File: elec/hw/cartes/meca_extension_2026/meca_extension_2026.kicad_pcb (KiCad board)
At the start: 4 copper layers, 126.2 x 84.5 mm, 189 parts, among them J1 2-1445051-3, J10 22053051, J11 B2B-XH-A, J12 22272021, J13 22053051, J14 22272031, J15 22272031, J16 5264-3P, J17 5267-3P, J18 5267-3P, J19 5267-3P, J2 B2B-XH-A, J20 5267-3P, J24 22053031, J25 22053031, J26 22053051, J27 22053041, J28 22053031, J29 22053031, J3 22272021, J4 22053051, J5 B2B-XH-A, J6 22272021, J7 22053051, J8 B2B-XH-A, J9 22272021, Q1 SI2310, Q10 SI2310, Q11 SI2310, Q12 2N7002, Q19 BSS84, Q2 SI2310, Q20 2N7002, Q3 2N7002, Q4 SI2310, Q5 SI2310, Q6 2N7002, Q7 SI2310, Q8 SI2310, Q9 2N7002, U1 TCA9548APWR, U11 LV14340DDAR, U2 PCA9535PW, U3 TLA2528IRTER, U4 TLV9061IDBVR, U5 TLV9061IDBVR, U6 TLV9061IDBVR, U7 TLV9061IDBVR, U8 74HCT238PW, U9 SN74LVC1T45DBV

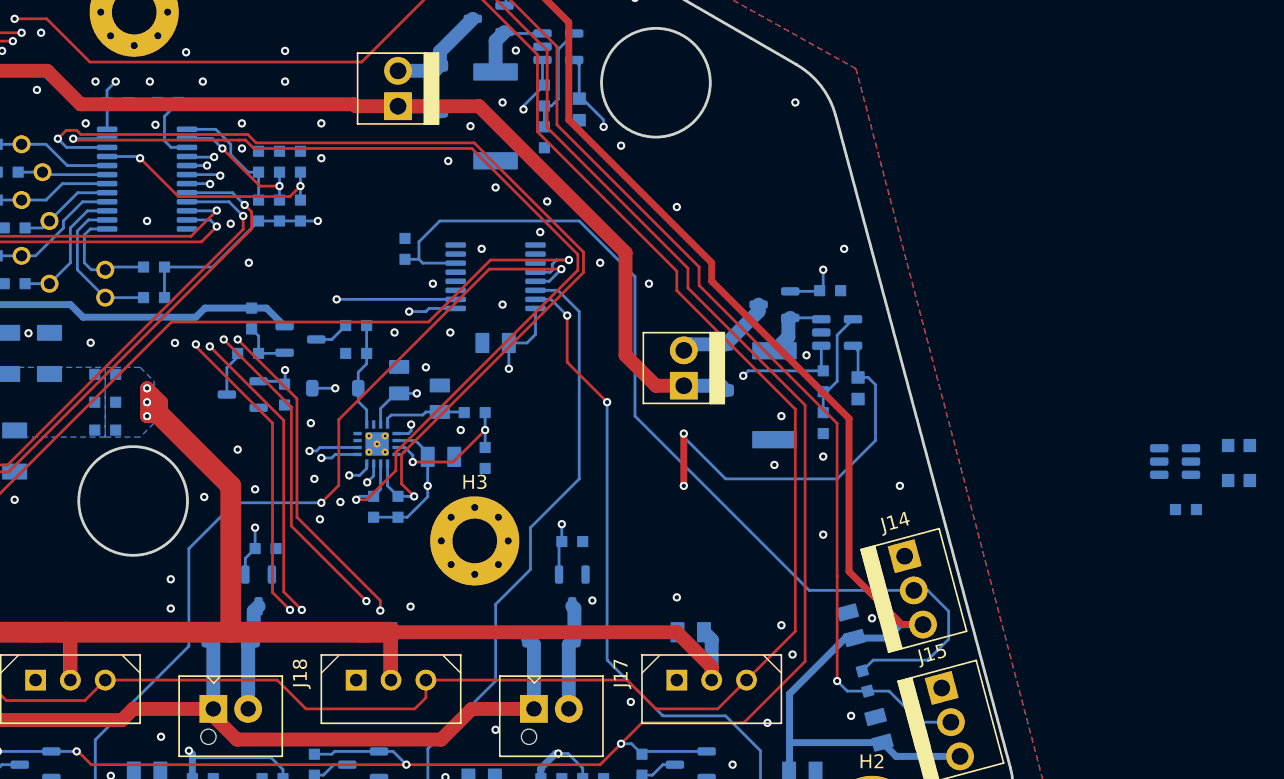
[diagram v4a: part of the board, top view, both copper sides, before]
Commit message: meca_extension : schematic correction and routing modified accordingly
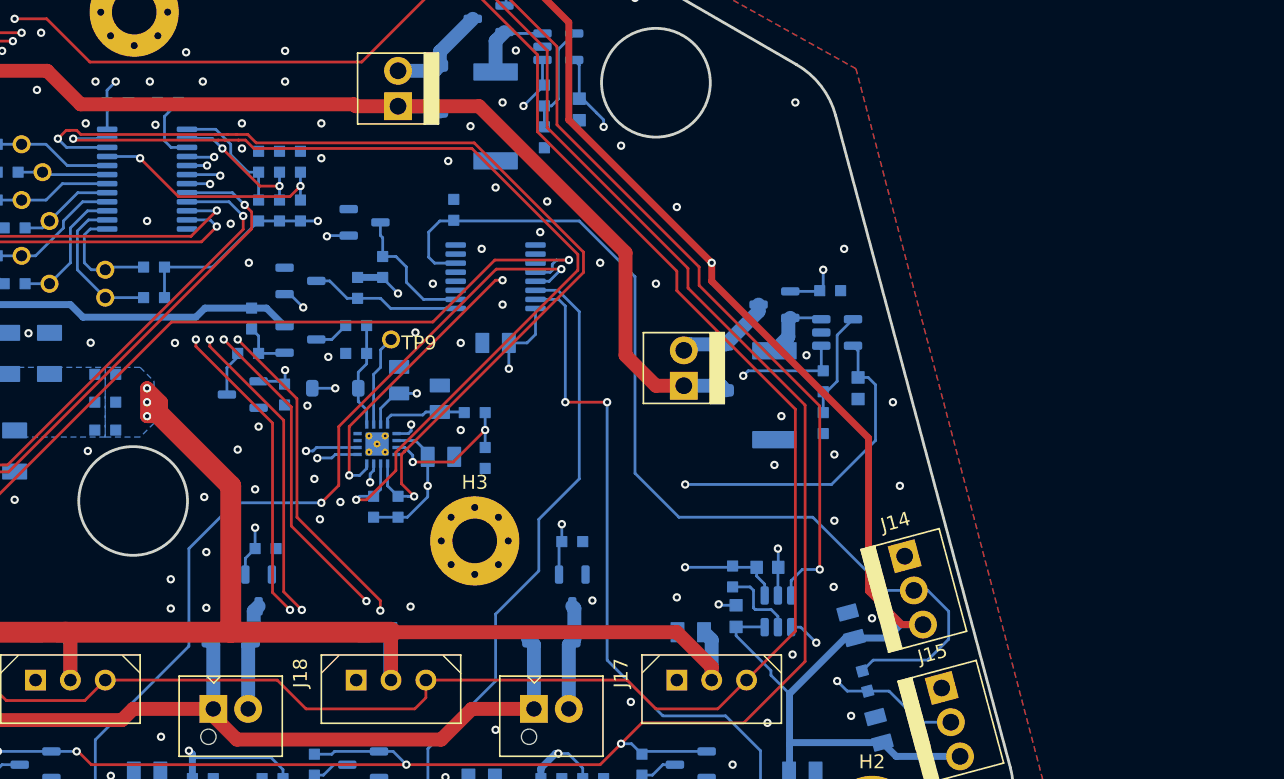
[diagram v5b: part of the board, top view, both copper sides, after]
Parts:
- added Q13: 2N7002, cocotter_transistors:SOT-23-3, B.Cu at (142.1, 84.1)
- added Q14: 2N7002, cocotter_transistors:SOT-23-3, B.Cu at (137.5, 88.3)
- added R63: 100k, cocotter_resistor:r0603_reflow, B.Cu at (143.4, 87.3)
- added R64: 100k, cocotter_resistor:r0603_reflow, B.Cu at (141.6, 88.8)
- added TP9: TestPoint, cocotter_others:testpoint-THT-0.8mm, F.Cu at (144.0, 92.5)
- moved C33 38.1 mm to (168.8, 112.3), turned to 90 degrees
- moved C34 34.4 mm to (171.0, 108.8), turned to 0 degrees
- moved R62 32.9 mm to (168.5, 109.5), turned to -90 degrees
- moved U9 30.5 mm to (171.8, 112.0), turned to -90 degrees
- moved R56 4.48 mm to (148.5, 83.2)
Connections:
- net /neopixel_cmd_0_3v3 renamed /neopixel_cmd_0_5v
- net /neopixel_cmd_1_3v3 renamed /neopixel_cmd_1_5v
- net /neopixel_cmd_2_3v3 renamed /neopixel_cmd_2_5v
- net /neopixel_cmd_3_3v3 renamed /neopixel_cmd_3_5v
- C11 pad 1: +3.3V -> +5V
- J14 pad 2: /neopixel_cmd_5v -> /neopixel_ret_5v
- R55 pad 2: /neopixel_cmd_5v -> /neopixel_ret_5v
- R56 pad 1: /neopixel_ret_3v3 -> /neopixel_ret_5v
- U3 pad 6: unconnected-(U3-AIN7/GPIO7-Pad6) -> Net-(U3-AIN7/GPIO7)
- U8 pad 1: /neopixel_sel_0_3v3 -> /neopixel_sel_0_5v
- U8 pad 16: +3.3V -> +5V
- U8 pad 2: /<NO NET> -> /neopixel_sel_1_5v
- U8 pad 6: /neopixel_ret_3v3 -> /neopixel_ret_5v
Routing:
- net /neopixel_ret_5v: track 0.00 -> 70.5 mm
- net /neopixel_ret_3v3: track 70.2 -> 0.00 mm
- net +5V: track 220.9 -> 266.6 mm, vias 0 -> 3
- net /neopixel_cmd_5v: track 0.00 -> 15.0 mm, vias 0 -> 2
- net /neopixel_cmd_3v3: track 107.6 -> 93.1 mm
- net /neopixel_sel_0_5v: track 0.00 -> 10.8 mm
- net /neopixel_sel_1_5v: track 0.00 -> 9.67 mm
- net Net-(U3-AIN7/GPIO7): track 0.00 -> 6.62 mm
- net Net-(U9-DIR): track 0.00 -> 5.63 mm
- net GND: track 6.18 -> 10.8 mm, vias 135 -> 142
- net /<NO NET>: track 69.7 -> 65.6 mm
- net +3.3V: track 198.5 -> 195.0 mm, vias 21 -> 20
- net /neopixel_sel_0_3v3: track 73.5 -> 70.4 mm
- net /neopixel_cmd_0_5v: track 47.2 -> 49.3 mm
- net /pump_current_1_3v3: track 38.9 -> 37.8 mm, vias 2 -> 3

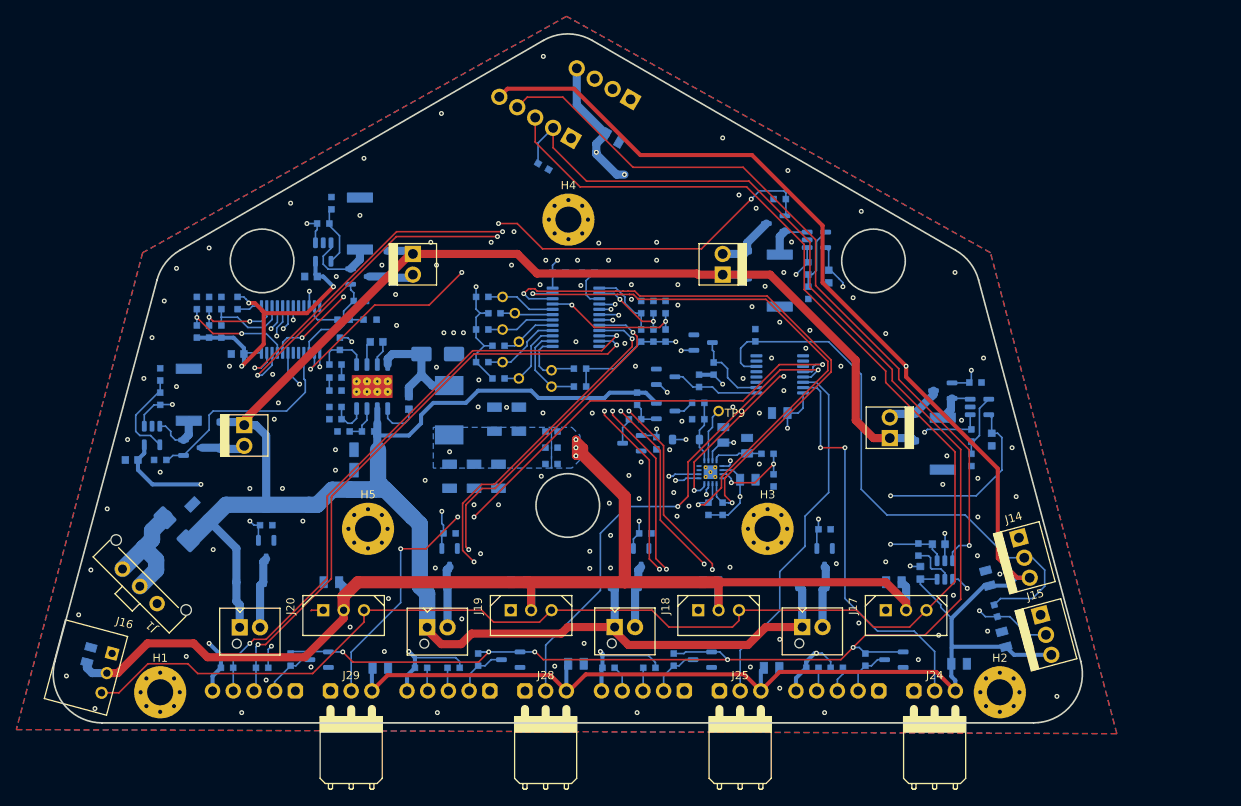
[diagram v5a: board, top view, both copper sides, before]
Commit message: meca extension: silkscreen modified, led moved
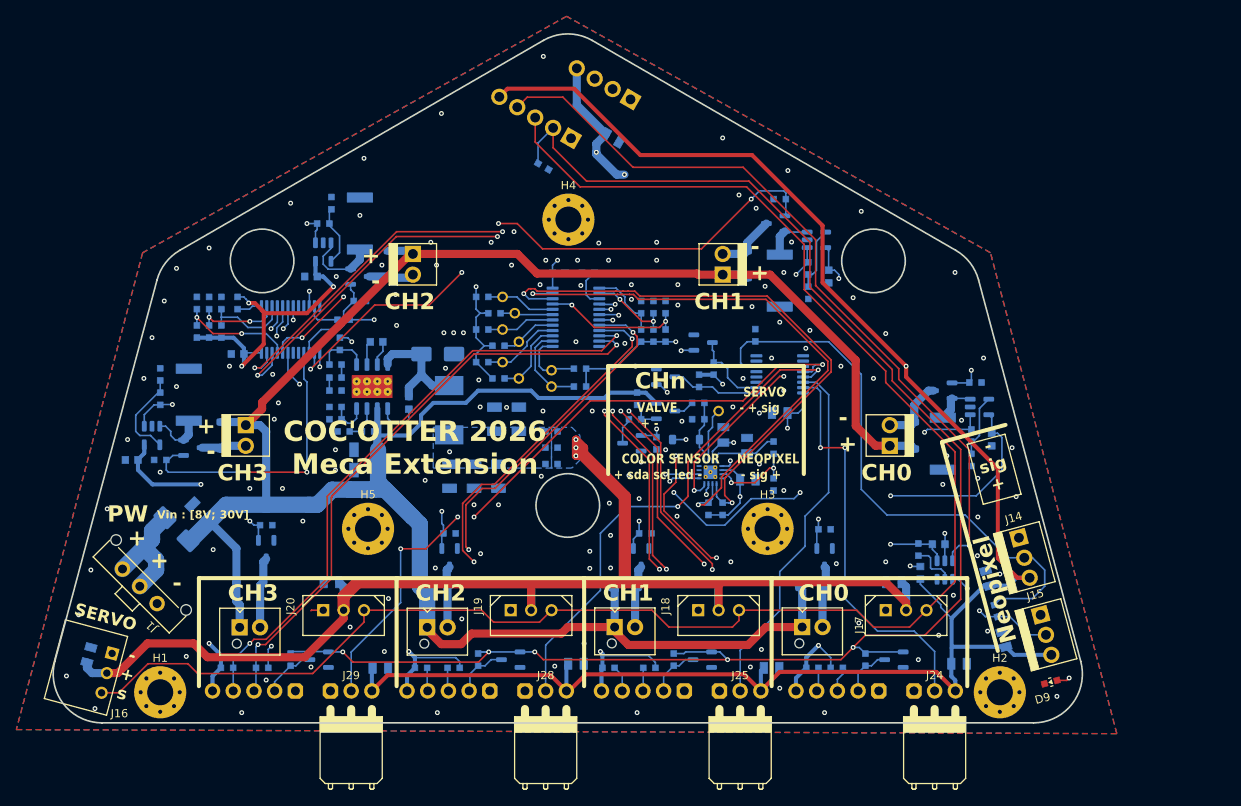
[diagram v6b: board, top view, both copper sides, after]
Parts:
- D9: moved to F.Cu
- TP9: moved to B.Cu
- moved D9 94.6 mm to (184.8, 125.8), turned to 15 degrees
- moved R17 1.06 mm to (150.8, 97.0), turned to -90 degrees
- moved D2 1.00 mm to (168.0, 95.5)
- moved J3 0.95 mm to (165.0, 95.5)
- moved R18 0.50 mm to (150.8, 101.5)
- moved J12 0.19 mm to (86.0, 95.5)
- turned TP9 to 180 degrees
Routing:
- net Net-(D9-PadA): track 1.70 -> 116.7 mm, vias 0 -> 4
- net /pmp_cmd_3_3v3: track 26.5 -> 35.7 mm, vias 0 -> 2
- net /pmp_cmd_0_3v3: track 109.0 -> 111.5 mm, vias 2 -> 4
- net Net-(U3-DECAP): track 6.14 -> 8.35 mm
- net Net-(D2-A): track 7.01 -> 8.34 mm
- net +BATT: track 309.1 -> 310.3 mm
- net /pump_current_2_3v3: track 71.1 -> 72.0 mm
- net /neopixel_sel_0_3v3: track 70.4 -> 69.8 mm
- net GND: vias 142 -> 141
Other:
- board text added: "+"
- board text added: "+3v3 sda scl gnd"
- board text added: "+5v ws2812 servo ColPwm gnd"
- board text added: "-"
- board text added: "- +"
- board text added: "- + s"
- board text added: "- sig +"
- board text added: "0"
- board text added: "0b0100.A2.A1.A0"
- board text added: "0b1110.A2.A1.A0"
- board text added: "1"
- board text added: "A0 A1 A2"
- board text added: "CH0"
- board text added: "CH1"
- board text added: "CH2"
- board text added: "CH3"
- board text added: "CHn"
- board text added: "COC'OTTER 2026 Meca Extension"
- board text added: "COLOR SENSOR + sda scl led -"
- board text added: "I2C"
- board text added: "NEOPIXEL - sig +"
- board text added: "Neopixel"
- board text added: "PCA9535PW"
- board text added: "PW"
- board text added: "Rh"
- board text added: "Rl"
- board text added: "SERVO"
- board text added: "SERVO - + sig"
- board text added: "TCA9548A:"
- board text added: "VALVE + -"
- board text added: "Vin : [8V; 30V]"
